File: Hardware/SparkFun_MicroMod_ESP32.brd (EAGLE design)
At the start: 22 x 22 mm, 55 parts, among them J1 MICROMOD-2222, Q2 MBT3904DW1T1, U1 W25QXX128MBIT-6X5, U2 ESP32, U4 CP2102N, Y1 40MHz, Y2 32.768kHz

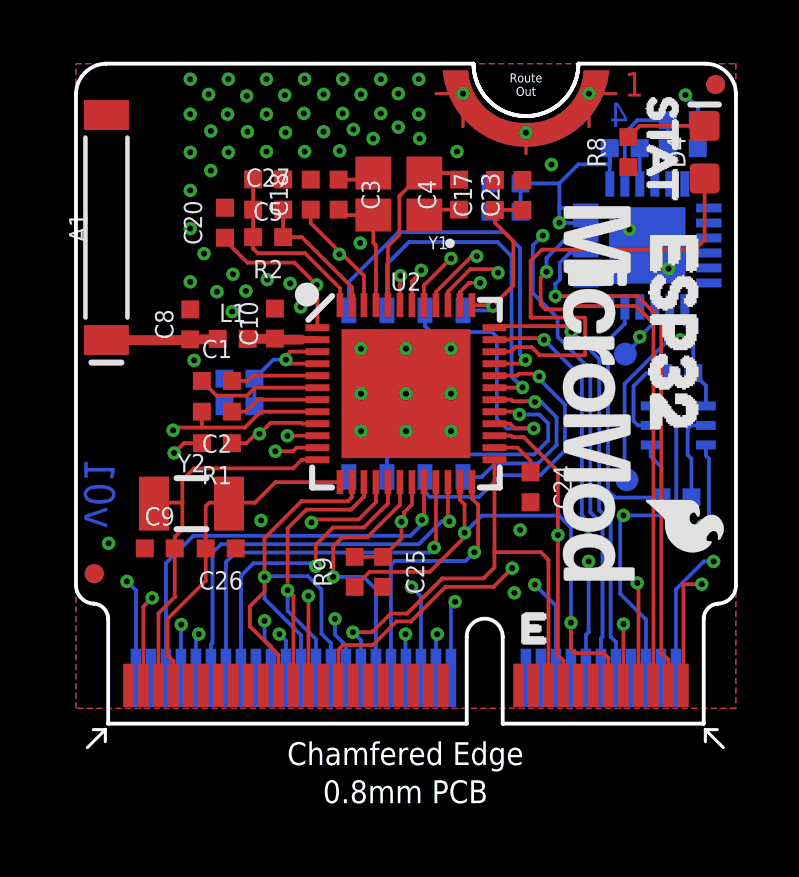
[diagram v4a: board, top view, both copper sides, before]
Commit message: v01 silk update
rotated the silk to line up with carrier boards
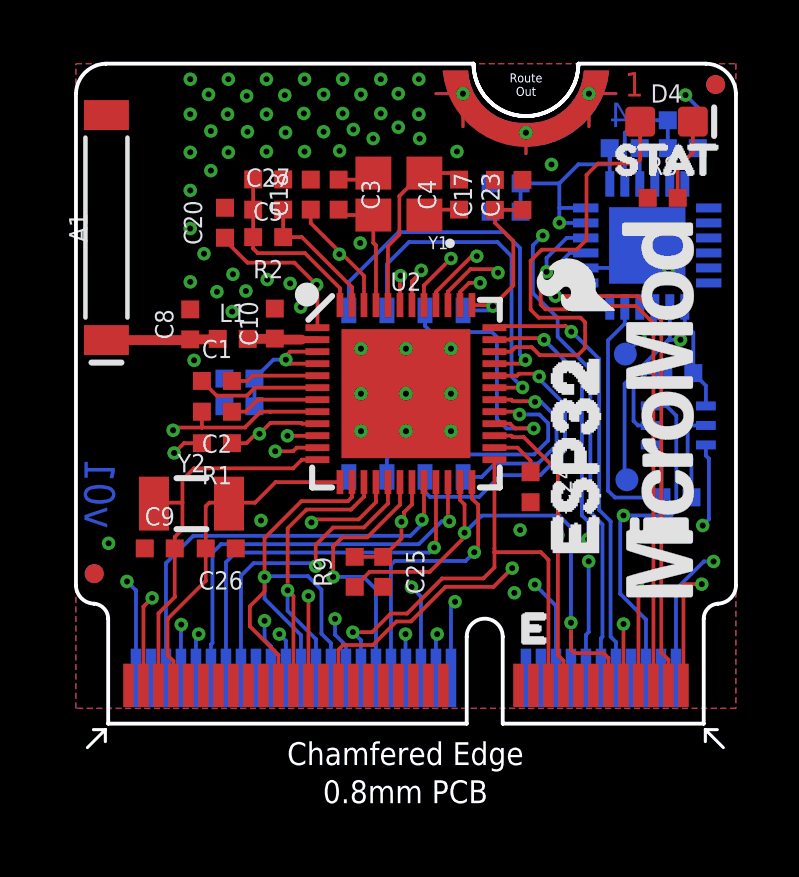
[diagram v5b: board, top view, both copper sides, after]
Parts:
- moved U$3 13.9 mm to (16.6, 4.24), turned to 90 degrees
- moved U$4 8.81 mm to (16.6, 14.6), turned to 90 degrees
- moved U$1 3.97 mm to (17.0, 18.8), turned to 0 degrees
- moved U$2 2.10 mm to (19.4, 10.5), turned to 90 degrees
- moved R8 1.91 mm to (19.6, 17.5), turned to 0 degrees
- moved D4 1.63 mm to (19.7, 20.1), turned to 0 degrees
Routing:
- net 5-STAT_LED: track 16.3 -> 15.3 mm
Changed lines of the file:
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@@
 <?xml version="1.0" encoding="utf-8"?>
 <!DOCTYPE eagle SYSTEM "eagle.dtd">
-<eagle version="9.6.0">
+<eagle version="9.5.2">
 <drawing>
 <settings>
@@
 <layer number="95" name="Names" color="7" fill="1" visible="no" active="no"/>
 <layer number="96" name="Values" color="7" fill="1" visible="no" active="no"/>
-<layer number="2" name="GND" color="16" fill="1" visible="no" active="yes"/>
+<layer number="2" name="GND" color="16" fill="1" visible="yes" active="yes"/>
 <layer number="3" name="Route3" color="17" fill="1" visible="no" active="no"/>
 <layer number="4" name="Route4" color="18" fill="1" visible="no" active="no"/>
@@
 <layer number="13" name="Route13" color="21" fill="1" visible="no" active="no"/>
 <layer number="14" name="Route14" color="22" fill="1" visible="no" active="no"/>
-<layer number="15" name="PWR" color="14" fill="1" visible="no" active="yes"/>
+<layer number="15" name="PWR" color="14" fill="1" visible="yes" active="yes"/>
 <layer number="53" name="tGND_GNDA" color="7" fill="9" visible="no" active="no"/>
 <layer number="54" name="bGND_GNDA" color="1" fill="9" visible="no" active="no"/>
@@
 <attribute name="VALUE" x="2.794" y="5.08" size="0.6096" layer="27" font="vector" ratio="20" align="top-center"/>
 </element>
-<element name="D4" library="SparkFun-LED" package="LED-0603" value="BLUE" x="20.955" y="19.05" smashed="yes" rot="R90">
-<attribute name="NAME" x="20.32" y="19.05" size="0.6096" layer="25" font="vector" ratio="20" rot="R90" align="bottom-center"/>
-<attribute name="PROD_ID" value="DIO-08575" x="81.915" y="38.1" size="1.778" layer="27" rot="R90" display="off"/>
-<attribute name="VALUE" x="21.59" y="19.05" size="0.6096" layer="27" font="vector" ratio="20" rot="R90" align="top-center"/>
+<element name="D4" library="SparkFun-LED" package="LED-0603" value="BLUE" x="19.685" y="20.066" smashed="yes">
+<attribute name="NAME" x="19.685" y="20.701" size="0.6096" layer="25" font="vector" ratio="20" align="bottom-center"/>
+<attribute name="PROD_ID" value="DIO-08575" x="38.735" y="-40.894" size="1.778" layer="27" display="off"/>
+<attribute name="VALUE" x="19.685" y="19.431" size="0.6096" layer="27" font="vector" ratio="20" align="top-center"/>
 </element>
 <element name="FRAME1" library="SparkFun-Aesthetics" package="CREATIVE_COMMONS" value="FRAME-LEDGER" x="-10.01" y="-23.06" smashed="yes">
@@
 <attribute name="VALUE" value="20k" x="6.407" y="16.979" size="0.6096" layer="27" font="vector" ratio="20" rot="R180" align="top-center"/>
 </element>
-<element name="R8" library="SparkFun-Resistors" package="0402-TIGHT" value="1k" x="18.415" y="19.05" smashed="yes" rot="R90">
-<attribute name="NAME" x="17.653" y="19.05" size="0.6096" layer="25" font="vector" ratio="20" rot="R90" align="bottom-center"/>
-<attribute name="PROD_ID" value="RES-14342" x="75.565" y="64.77" size="1.778" layer="27" rot="R90" display="off"/>
-<attribute name="VALUE" value="1k" x="19.177" y="19.05" size="0.6096" layer="27" font="vector" ratio="20" rot="R90" align="top-center"/>
+<element name="R8" library="SparkFun-Resistors" package="0402-TIGHT" value="1k" x="19.558" y="17.526" smashed="yes">
+<attribute name="NAME" x="19.558" y="18.288" size="0.6096" layer="25" font="vector" ratio="20" align="bottom-center"/>
+<attribute name="PROD_ID" value="RES-14342" x="65.278" y="-39.624" size="1.778" layer="27" display="off"/>
+<attribute name="VALUE" value="1k" x="19.558" y="16.764" size="0.6096" layer="27" font="vector" ratio="20" align="top-center"/>
 </element>
 <element name="R9" library="SparkFun-Resistors" package="0402-TIGHT" value="10k" x="9.291" y="5.061" smashed="yes" rot="R90">
@@
 <element name="FD4" library="SparkFun-Aesthetics" package="FIDUCIAL-MICRO" value="FIDUCIALUFIDUCIAL" x="21.323" y="21.303" smashed="yes"/>
 <element name="LOGO1" library="SparkFun-Aesthetics" package="ORDERING_INSTRUCTIONS" value="SPECIAL_INSTRUCTIONS-ORDERING" x="30.48" y="50.8" smashed="yes"/>
-<element name="U$1" library="buzzard_labels" package="STAT0" value="" x="19.558" y="21.844" smashed="yes" rot="R270"/>
-<element name="U$3" library="buzzard_labels (1)" package="ESP321" value="" x="19.939" y="17.7292" smashed="yes" rot="R270"/>
-<element name="U$2" library="SparkFun-MicroMod" package="MICROMOD_LOGO_.5" value="" x="17.399" y="11" smashed="yes" rot="R270"/>
-<element name="U$4" library="SparkFun-Aesthetics" package="SFE_LOGO_FLAME_.1" value="" x="20.32" y="6.604" smashed="yes" rot="R270"/>
+<element name="U$1" library="buzzard_labels" package="STAT0" value="" x="17.018" y="18.796" smashed="yes"/>
+<element name="U$3" library="buzzard_labels (1)" package="ESP321" value="" x="16.637" y="4.2418" smashed="yes" rot="R90"/>
+<element name="U$2" library="SparkFun-MicroMod" package="MICROMOD_LOGO_.5" value="" x="19.431" y="10.463" smashed="yes" rot="R90"/>
+<element name="U$4" library="SparkFun-Aesthetics" package="SFE_LOGO_FLAME_.1" value="" x="16.637" y="14.605" smashed="yes" rot="R90"/>
 <element name="U$6" library="SparkFun-MicroMod" package="MICROMOD_LOGO_.5" value="" x="7.8232" y="5.9436" smashed="yes" rot="MR0"/>
 <element name="U$7" library="buzzard_labels (1)" package="ESP321" value="" x="9.4234" y="8.6868" smashed="yes" rot="MR0"/>
@@
 <wire x1="17.5508" y1="6.6431" x2="17.1444" y2="7.0495" width="0.127" layer="16"/>
 <via x="15.56" y="16.27" extent="1-16" drill="0.2"/>
-<wire x1="15.56" y1="16.27" x2="15.3" y2="16.53" width="0.127" layer="15"/>
-<wire x1="15.3" y1="16.53" x2="12.13" y2="16.53" width="0.127" layer="15"/>
+<wire x1="15.56" y1="16.27" x2="15.173" y2="16.657" width="0.127" layer="15"/>
+<wire x1="15.173" y1="16.657" x2="12.257" y2="16.657" width="0.127" layer="15"/>
 <wire x1="11.51" y1="15.11" x2="11.51" y2="15.91" width="0.127" layer="15"/>
-<wire x1="12.13" y1="16.53" x2="11.51" y2="15.91" width="0.127" layer="15"/>
+<wire x1="12.257" y1="16.657" x2="11.51" y2="15.91" width="0.127" layer="15"/>
 <wire x1="15.2292" y1="14.3504" x2="16.057" y2="13.5226" width="0.127" layer="16"/>
 <wire x1="16.057" y1="13.5226" x2="16.057" y2="12.8951625" width="0.127" layer="16"/>
@@
 <wire x1="14.648" y1="12.5482" x2="15.1934" y2="12.5482" width="0.127" layer="1"/>
 <wire x1="15.1934" y1="12.5482" x2="15.4607" y2="12.2809" width="0.127" layer="1"/>
-<wire x1="15.4607" y1="12.2809" x2="16.97" y2="12.2809" width="0.127" layer="1"/>
-<wire x1="16.97" y1="12.2809" x2="16.97" y2="13.5172" width="0.127" layer="1"/>
-<wire x1="16.97" y1="13.5172" x2="16.9542" y2="13.533" width="0.127" layer="1"/>
-<wire x1="16.9542" y1="13.533" x2="15.1798" y2="13.533" width="0.127" layer="1"/>
-<wire x1="15.1798" y1="13.533" x2="15.1549" y2="13.5579" width="0.127" layer="1"/>
-<wire x1="15.1549" y1="15.4253" x2="15.5298" y2="15.8002" width="0.127" layer="1"/>
-<wire x1="15.5298" y1="15.8002" x2="20.6302" y2="15.8002" width="0.127" layer="1"/>
-<wire x1="20.6302" y1="15.8002" x2="20.955" y2="16.125" width="0.127" layer="1"/>
-<wire x1="20.955" y1="16.125" x2="20.955" y2="18.173" width="0.127" layer="1"/>
-<wire x1="15.1549" y1="13.5579" x2="15.1549" y2="15.4253" width="0.127" layer="1"/>
+<wire x1="15.4607" y1="12.2809" x2="16.7259" y2="12.2809" width="0.127" layer="1"/>
+<wire x1="16.7259" y1="12.2809" x2="16.97" y2="12.525" width="0.127" layer="1"/>
+<wire x1="16.97" y1="12.525" x2="16.97" y2="13.383" width="0.127" layer="1"/>
+<wire x1="16.97" y1="13.383" x2="16.82" y2="13.533" width="0.127" layer="1"/>
+<wire x1="16.82" y1="13.533" x2="15.423" y2="13.533" width="0.127" layer="1"/>
+<wire x1="15.423" y1="13.533" x2="15.1549" y2="13.8011" width="0.127" layer="1"/>
+<wire x1="15.1549" y1="13.8011" x2="15.1549" y2="15.4253" width="0.127" layer="1"/>
+<wire x1="15.5298" y1="15.8002" x2="15.1549" y2="15.4253" width="0.127" layer="1"/>
+<wire x1="18.808" y1="20.066" x2="18.808" y2="18.808" width="0.127" layer="1"/>
+<wire x1="18.808" y1="18.808" x2="18.669" y2="18.669" width="0.127" layer="1"/>
+<wire x1="18.669" y1="18.669" x2="17.399" y2="18.669" width="0.127" layer="1"/>
+<wire x1="17.399" y1="18.669" x2="17.018" y2="18.288" width="0.127" layer="1"/>
+<wire x1="17.018" y1="18.288" x2="17.018" y2="16.129" width="0.127" layer="1"/>
+<wire x1="16.6892" y1="15.8002" x2="15.5298" y2="15.8002" width="0.127" layer="1"/>
+<wire x1="17.018" y1="16.129" x2="16.6892" y2="15.8002" width="0.127" layer="1"/>
 </signal>
 <signal name="2-SPI_MISO/SD_DATA0">
@@
 <contactref element="R8" pad="2"/>
 <contactref element="D4" pad="C"/>
-<wire x1="18.415" y1="19.55" x2="18.792" y2="19.927" width="0.127" layer="1"/>
-<wire x1="18.792" y1="19.927" x2="20.955" y2="19.927" width="0.127" layer="1"/>
+<wire x1="20.562" y1="20.066" x2="20.562" y2="19.038" width="0.127" layer="1"/>
+<wire x1="20.058" y1="18.534" x2="20.058" y2="17.526" width="0.127" layer="1"/>
+<wire x1="20.562" y1="19.038" x2="20.058" y2="18.534" width="0.127" layer="1"/>
 </signal>
 <signal name="N$4">

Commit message: v02
- Replaced antenna inductor with 0 ohm resistor
- Replaced Flash IC VDD supply from 3.3V power rail to ESP32's FLASH_VDD pin.
- Replaced edge connector to updated pinout
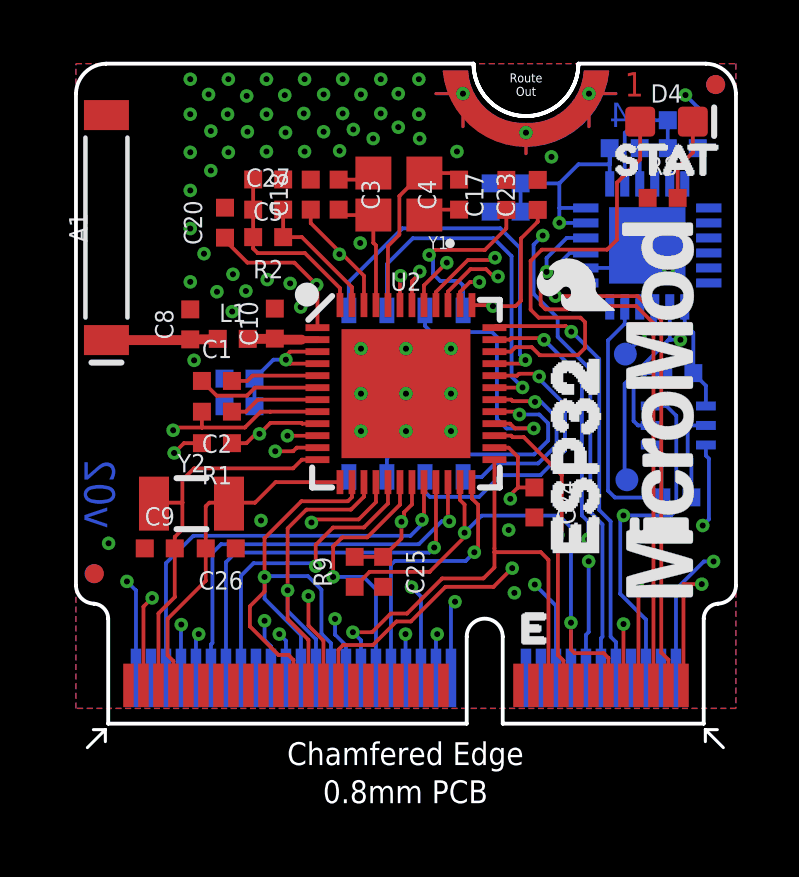
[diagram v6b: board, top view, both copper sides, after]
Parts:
- L1: value 2.7nH -> 0; device SparkFun-Coils:0402-TIGHT -> SparkFun-Resistors:0402-TIGHT
- moved C24 0.52 mm to (15.3, 7.37)
- moved C23 0.51 mm to (15.4, 17.6)
- moved C17 0.38 mm to (14.3, 17.6)
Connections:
- net 25-G4/AUD_LRCLK/SCL1: now also J1.53; no longer J1.55
- net 26-G5/AUD_BCLK/SDA1: now also J1.51; no longer J1.53
- net 3.3V: no longer C17.1, U1.8
- net 39-BATT/3: now also J1.49; no longer J1.51
- net FLASH_VDD: now also C17.1, U1.8
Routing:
- net FLASH_VDD: track 1.77 -> 18.4 mm, vias 0 -> 2
- net 3.3V: track 43.0 -> 41.5 mm
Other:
- board text added: "v02"
- board text removed: "v01"
